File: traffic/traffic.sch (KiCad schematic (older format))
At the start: 7 parts, among them J1 Conn_01x06_Male

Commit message: changed LEds from 3mm to 5mm;added Status LED to motor-module
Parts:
- D1: renamed from D5; footprint LEDs:LED_D3.0mm -> LEDs:LED_D5.0mm
- D2: renamed from D4; footprint LEDs:LED_D3.0mm -> LEDs:LED_D5.0mm
- D3: renamed from D1; footprint LEDs:LED_D3.0mm -> LEDs:LED_D5.0mm
- D4: renamed from D3; footprint LEDs:LED_D3.0mm -> LEDs:LED_D5.0mm
- D5: renamed from D2; footprint LEDs:LED_D3.0mm -> LEDs:LED_D5.0mm
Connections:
- net labels added: +5C
- net labels removed: GND
- wire segments 23 -> 24
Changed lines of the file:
@@
 EESchema Schematic File Version 4
-LIBS:openplc_modules-cache
+LIBS:traffic-cache
 EELAYER 26 0
 EELAYER END
@@
 $EndDescr
 $Comp
-L Device:LED D5
+L Device:LED D1
 U 1 1 5C2C2999
 P 5200 4100
-F 0 "D5" H 5191 4316 50  0000 C CNN
+F 0 "D1" H 5191 4316 50  0000 C CNN
 F 1 "LED" H 5191 4225 50  0000 C CNN
-F 2 "LEDs:LED_D3.0mm" H 5200 4100 50  0001 C CNN
+F 2 "LEDs:LED_D5.0mm" H 5200 4100 50  0001 C CNN
 F 3 "~" H 5200 4100 50  0001 C CNN
 	1    5200 4100
@@
 $EndComp
 $Comp
-L Device:LED D2
+L Device:LED D5
 U 1 1 5C2C2A10
 P 5200 3050
-F 0 "D2" H 5191 3266 50  0000 C CNN
+F 0 "D5" H 5191 3266 50  0000 C CNN
 F 1 "LED" H 5191 3175 50  0000 C CNN
-F 2 "LEDs:LED_D3.0mm" H 5200 3050 50  0001 C CNN
+F 2 "LEDs:LED_D5.0mm" H 5200 3050 50  0001 C CNN
 F 3 "~" H 5200 3050 50  0001 C CNN
 	1    5200 3050
@@
 $EndComp
 $Comp
-L Device:LED D4
+L Device:LED D2
 U 1 1 5C2C2A3E
 P 5200 3750
-F 0 "D4" H 5191 3966 50  0000 C CNN
+F 0 "D2" H 5191 3966 50  0000 C CNN
 F 1 "LED" H 5191 3875 50  0000 C CNN
-F 2 "LEDs:LED_D3.0mm" H 5200 3750 50  0001 C CNN
+F 2 "LEDs:LED_D5.0mm" H 5200 3750 50  0001 C CNN
 F 3 "~" H 5200 3750 50  0001 C CNN
 	1    5200 3750
@@
 $EndComp
 $Comp
-L Device:LED D3
+L Device:LED D4
 U 1 1 5C2C2A6F
 P 5200 3400
-F 0 "D3" H 5191 3616 50  0000 C CNN
+F 0 "D4" H 5191 3616 50  0000 C CNN
 F 1 "LED" H 5191 3525 50  0000 C CNN
-F 2 "LEDs:LED_D3.0mm" H 5200 3400 50  0001 C CNN
+F 2 "LEDs:LED_D5.0mm" H 5200 3400 50  0001 C CNN
 F 3 "~" H 5200 3400 50  0001 C CNN
 	1    5200 3400
@@
 $EndComp
 $Comp
-L Device:LED D1
+L Device:LED D3
 U 1 1 5C2C2AD6
 P 5200 2700
-F 0 "D1" H 5191 2916 50  0000 C CNN
+F 0 "D3" H 5191 2916 50  0000 C CNN
 F 1 "LED" H 5191 2825 50  0000 C CNN
-F 2 "LEDs:LED_D3.0mm" H 5200 2700 50  0001 C CNN
+F 2 "LEDs:LED_D5.0mm" H 5200 2700 50  0001 C CNN
 F 3 "~" H 5200 2700 50  0001 C CNN
 	1    5200 2700
@@
 	1    0    0    -1
 $EndComp
-$Comp
-L power:GND #PWR0101
-U 1 1 5C2C3C39
-P 5050 4900
-F 0 "#PWR0101" H 5050 4650 50  0001 C CNN
-F 1 "GND" H 5055 4727 50  0000 C CNN
-F 2 "" H 5050 4900 50  0001 C CNN
-F 3 "" H 5050 4900 50  0001 C CNN
-	1    5050 4900
-	1    0    0    -1
-$EndComp
 Wire Wire Line
 	5050 4750 5050 4800
@@
 Wire Wire Line
 	5050 3750 5050 4100
+$Comp
+L power:+5C #PWR?
+U 1 1 5C32F085
+P 4700 4900
+F 0 "#PWR?" H 4700 4750 50  0001 C CNN
+F 1 "+5C" H 4715 5073 50  0000 C CNN
+F 2 "" H 4700 4900 50  0001 C CNN
+F 3 "" H 4700 4900 50  0001 C CNN
+	1    4700 4900
+	1    0    0    -1
+$EndComp
+Wire Wire Line
+	4700 4900 5050 4900
 $EndSCHEMATC

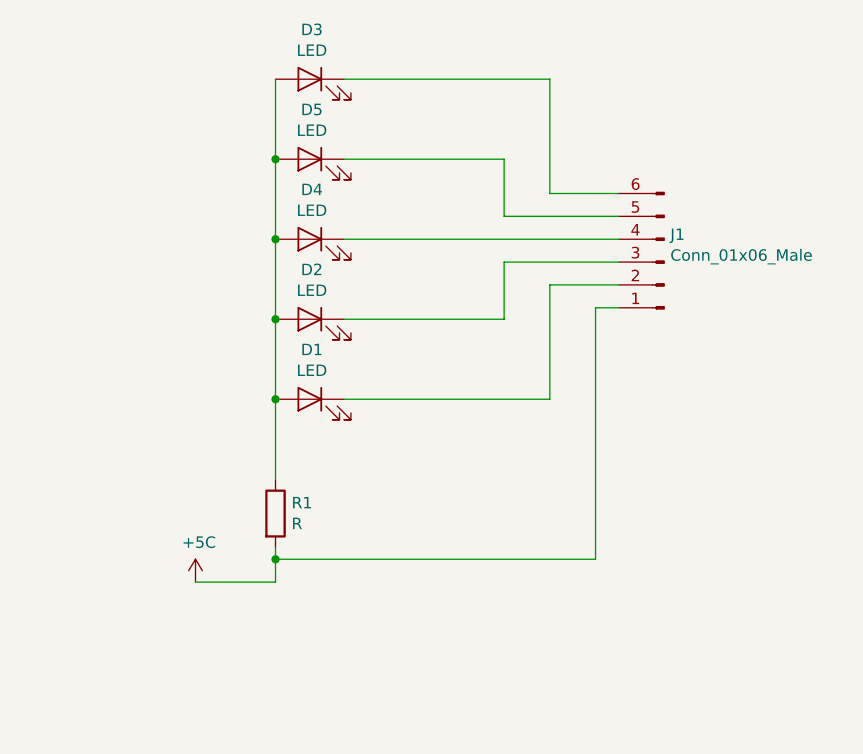
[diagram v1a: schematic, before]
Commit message: mounting holes in motor, extra pins in traffic, corrections in labels
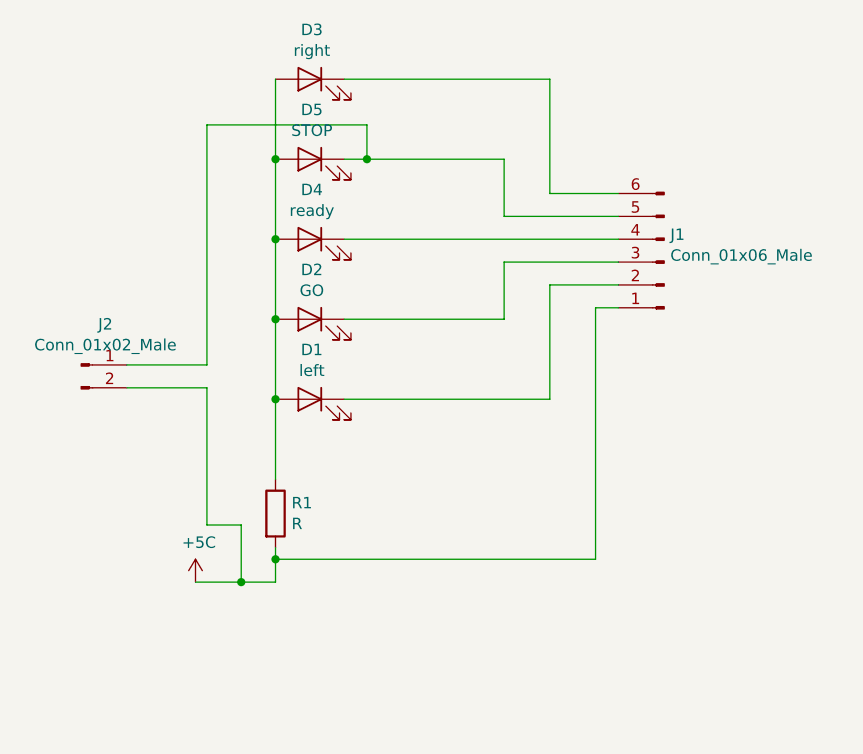
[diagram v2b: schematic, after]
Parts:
- added J2: Conn_01x02_Male, Socket_Strips:Socket_Strip_Straight_1x02_Pitch2.54mm, symbol Connector:Conn_01x02_Male
- D1: value LED -> left
- D2: value LED -> GO
- D3: value LED -> right
- D4: value LED -> ready
- D5: value LED -> STOP
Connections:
- net +5C: now also J2.2 (Pin_2)
- net at D5.1 (K), J1.5 (Pin_5): now also J2.1 (Pin_1)
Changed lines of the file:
@@
 P 5200 4100
 F 0 "D1" H 5191 4316 50  0000 C CNN
-F 1 "LED" H 5191 4225 50  0000 C CNN
+F 1 "left" H 5191 4225 50  0000 C CNN
 F 2 "LEDs:LED_D5.0mm" H 5200 4100 50  0001 C CNN
 F 3 "~" H 5200 4100 50  0001 C CNN
@@
 P 5200 3050
 F 0 "D5" H 5191 3266 50  0000 C CNN
-F 1 "LED" H 5191 3175 50  0000 C CNN
+F 1 "STOP" H 5191 3175 50  0000 C CNN
 F 2 "LEDs:LED_D5.0mm" H 5200 3050 50  0001 C CNN
 F 3 "~" H 5200 3050 50  0001 C CNN
@@
 P 5200 3750
 F 0 "D2" H 5191 3966 50  0000 C CNN
-F 1 "LED" H 5191 3875 50  0000 C CNN
+F 1 "GO" H 5191 3875 50  0000 C CNN
 F 2 "LEDs:LED_D5.0mm" H 5200 3750 50  0001 C CNN
 F 3 "~" H 5200 3750 50  0001 C CNN
@@
 P 5200 3400
 F 0 "D4" H 5191 3616 50  0000 C CNN
-F 1 "LED" H 5191 3525 50  0000 C CNN
+F 1 "ready" H 5191 3525 50  0000 C CNN
 F 2 "LEDs:LED_D5.0mm" H 5200 3400 50  0001 C CNN
 F 3 "~" H 5200 3400 50  0001 C CNN
@@
 P 5200 2700
 F 0 "D3" H 5191 2916 50  0000 C CNN
-F 1 "LED" H 5191 2825 50  0000 C CNN
+F 1 "right" H 5191 2825 50  0000 C CNN
 F 2 "LEDs:LED_D5.0mm" H 5200 2700 50  0001 C CNN
 F 3 "~" H 5200 2700 50  0001 C CNN
@@
 	6250 3200 6550 3200
 Wire Wire Line
-	5350 3050 6050 3050
+	5350 3050 5450 3050
 Wire Wire Line
 	6050 3050 6050 3300
@@
 	5050 3750 5050 4100
 $Comp
-L power:+5C #PWR?
+L power:+5C #PWR0101
 U 1 1 5C32F085
 P 4700 4900
-F 0 "#PWR?" H 4700 4750 50  0001 C CNN
+F 0 "#PWR0101" H 4700 4750 50  0001 C CNN
 F 1 "+5C" H 4715 5073 50  0000 C CNN
 F 2 "" H 4700 4900 50  0001 C CNN
@@
 $EndComp
 Wire Wire Line
-	4700 4900 5050 4900
+	4700 4900 4900 4900
+$Comp
+L Connector:Conn_01x02_Male J2
+U 1 1 5C3CB942
+P 4200 3950
+F 0 "J2" H 4306 4128 50  0000 C CNN
+F 1 "Conn_01x02_Male" H 4306 4037 50  0000 C CNN
+F 2 "Socket_Strips:Socket_Strip_Straight_1x02_Pitch2.54mm" H 4200 3950 50  0001 C CNN
+F 3 "~" H 4200 3950 50  0001 C CNN
+	1    4200 3950
+	1    0    0    -1
+$EndComp
+Wire Wire Line
+	4400 4050 4750 4050
+Wire Wire Line
+	4750 4050 4750 4650
+Wire Wire Line
+	4750 4650 4900 4650
+Wire Wire Line
+	4900 4650 4900 4900
+Connection ~ 4900 4900
+Wire Wire Line
+	4900 4900 5050 4900
+Wire Wire Line
+	4400 3950 4750 3950
+Wire Wire Line
+	4750 2900 5450 2900
+Wire Wire Line
+	5450 2900 5450 3050
+Wire Wire Line
+	4750 2900 4750 3950
+Connection ~ 5450 3050
+Wire Wire Line
+	5450 3050 6050 3050
 $EndSCHEMATC

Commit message: gerbers generate
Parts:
- added Q?: BC327, Package_TO_SOT_THT:TO-92_Inline, symbol Transistor_BJT:BC327
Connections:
- net +5C: now also Q?.3 (E); no longer J1.1 (Pin_1), R1.2
- new net: Q?.1 (C), R1.2
- new net: J1.1 (Pin_1), Q?.2 (B)
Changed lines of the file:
@@
 	1    0    0    -1
 $EndComp
-Wire Wire Line
-	5050 4750 5050 4800
 $Comp
 L Connector:Conn_01x06_Male J1
@@
 	-1   0    0    1
 $EndComp
-Wire Wire Line
-	5050 4800 6450 4800
-Wire Wire Line
-	6450 4800 6450 3700
-Connection ~ 5050 4800
-Wire Wire Line
-	5050 4800 5050 4900
 Wire Wire Line
 	6550 3700 6450 3700
@@
 	1    0    0    -1
 $EndComp
-Wire Wire Line
-	4700 4900 4900 4900
 $Comp
 L Connector:Conn_01x02_Male J2
@@
 	4400 4050 4750 4050
 Wire Wire Line
-	4750 4050 4750 4650
-Wire Wire Line
-	4750 4650 4900 4650
-Wire Wire Line
-	4900 4650 4900 4900
-Connection ~ 4900 4900
-Wire Wire Line
-	4900 4900 5050 4900
-Wire Wire Line
 	4400 3950 4750 3950
 Wire Wire Line
@@
 Wire Wire Line
 	5450 3050 6050 3050
+Wire Wire Line
+	6450 3700 6450 5150
+Wire Wire Line
+	6450 5150 5350 5150
+Wire Wire Line
+	5050 4750 5050 4950
+Wire Wire Line
+	4700 4900 4700 5500
+Wire Wire Line
+	4700 5500 5050 5500
+Wire Wire Line
+	5050 5500 5050 5350
+Connection ~ 4700 4900
+Wire Wire Line
+	4700 4900 4750 4900
+Wire Wire Line
+	4750 4050 4750 4900
+$Comp
+L Transistor_BJT:BC327 Q?
+U 1 1 5C480656
+P 5150 5150
+F 0 "Q?" H 5340 5196 50  0000 L CNN
+F 1 "BC327" H 5340 5105 50  0000 L CNN
+F 2 "Package_TO_SOT_THT:TO-92_Inline" H 5350 5075 50  0001 L CIN
+F 3 "http://www.onsemi.com/pub_link/Collateral/BC327-D.PDF" H 5150 5150 50  0001 L CNN
+	1    5150 5150
+	-1   0    0    -1
+$EndComp
 $EndSCHEMATC

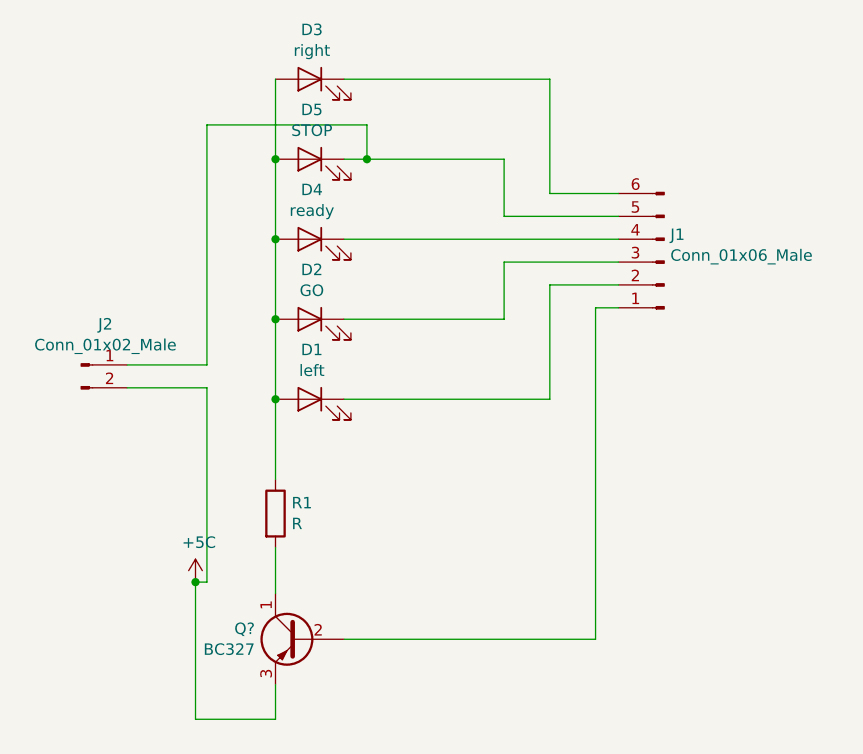
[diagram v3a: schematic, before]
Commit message: transistor driving in traffic light; updated the BOM and gerbers accordingly
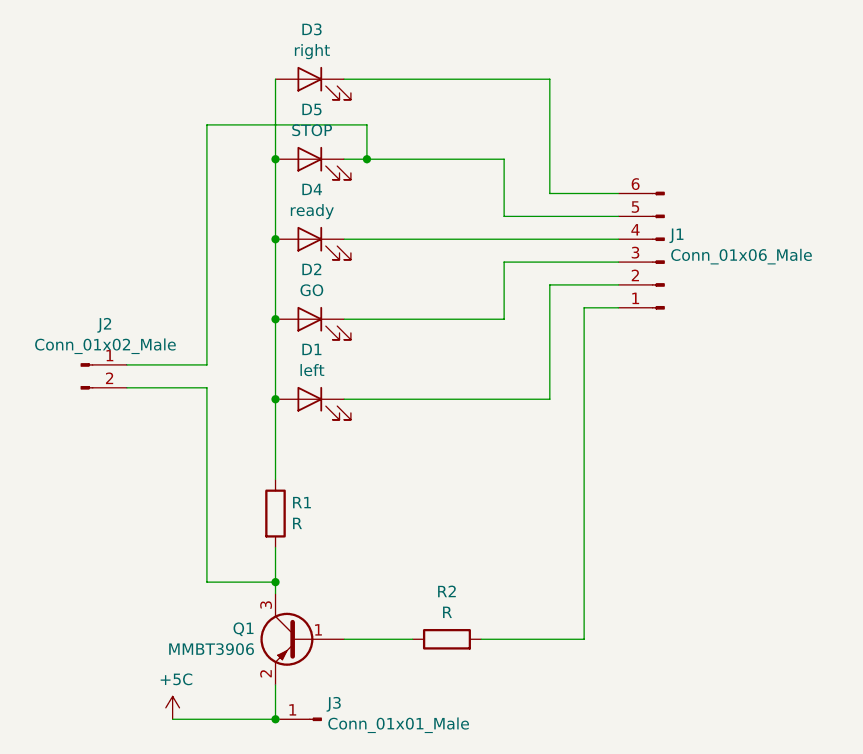
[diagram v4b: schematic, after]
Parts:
- removed Q?: BC327, Package_TO_SOT_THT:TO-92_Inline, symbol Transistor_BJT:BC327
- added J3: Conn_01x01_Male, Socket_Strips:Socket_Strip_Straight_1x01_Pitch2.54mm, symbol Connector:Conn_01x01_Male
- added Q1: MMBT3906, TO_SOT_Packages_SMD:SOT-23, symbol Transistor_BJT:MMBT3906
- added R2: R, Resistors_SMD:R_0603_HandSoldering, symbol Device:R
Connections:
- net +5C: now also J3.1 (Pin_1), Q1.2 (E); no longer J2.2 (Pin_2)
- net at R1.2: now also J2.2 (Pin_2), Q1.3 (C)
- net at J1.1 (Pin_1): now also R2.2
- new net: Q1.1 (B), R2.1
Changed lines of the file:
@@
 	1    0    0    -1
 $EndComp
-$Comp
-L Connector:Conn_01x06_Male J1
-U 1 1 5C2C6811
-P 6750 3500
-F 0 "J1" H 6723 3380 50  0000 R CNN
-F 1 "Conn_01x06_Male" H 6723 3471 50  0000 R CNN
-F 2 "Socket_Strips:Socket_Strip_Straight_1x06_Pitch2.54mm" H 6750 3500 50  0001 C CNN
-F 3 "~" H 6750 3500 50  0001 C CNN
-	1    6750 3500
-	-1   0    0    1
-$EndComp
-Wire Wire Line
-	6550 3700 6450 3700
 Connection ~ 5050 4100
 Wire Wire Line
@@
 L power:+5C #PWR0101
 U 1 1 5C32F085
-P 4700 4900
-F 0 "#PWR0101" H 4700 4750 50  0001 C CNN
-F 1 "+5C" H 4715 5073 50  0000 C CNN
-F 2 "" H 4700 4900 50  0001 C CNN
-F 3 "" H 4700 4900 50  0001 C CNN
-	1    4700 4900
+P 4600 5500
+F 0 "#PWR0101" H 4600 5350 50  0001 C CNN
+F 1 "+5C" H 4615 5673 50  0000 C CNN
+F 2 "" H 4600 5500 50  0001 C CNN
+F 3 "" H 4600 5500 50  0001 C CNN
+	1    4600 5500
 	1    0    0    -1
 $EndComp
@@
 	5450 3050 6050 3050
 Wire Wire Line
-	6450 3700 6450 5150
-Wire Wire Line
-	6450 5150 5350 5150
-Wire Wire Line
-	5050 4750 5050 4950
-Wire Wire Line
-	4700 4900 4700 5500
-Wire Wire Line
-	4700 5500 5050 5500
+	5050 4750 5050 4900
 Wire Wire Line
 	5050 5500 5050 5350
-Connection ~ 4700 4900
-Wire Wire Line
-	4700 4900 4750 4900
 Wire Wire Line
 	4750 4050 4750 4900
+Wire Wire Line
+	4750 4900 5050 4900
+Connection ~ 5050 4900
+Wire Wire Line
+	5050 4900 5050 4950
+Wire Wire Line
+	4600 5500 5050 5500
 $Comp
-L Transistor_BJT:BC327 Q?
-U 1 1 5C480656
+L Transistor_BJT:MMBT3906 Q1
+U 1 1 5C485559
 P 5150 5150
-F 0 "Q?" H 5340 5196 50  0000 L CNN
-F 1 "BC327" H 5340 5105 50  0000 L CNN
-F 2 "Package_TO_SOT_THT:TO-92_Inline" H 5350 5075 50  0001 L CIN
-F 3 "http://www.onsemi.com/pub_link/Collateral/BC327-D.PDF" H 5150 5150 50  0001 L CNN
+F 0 "Q1" H 5340 5196 50  0000 L CNN
+F 1 "MMBT3906" H 5340 5105 50  0000 L CNN
+F 2 "TO_SOT_Packages_SMD:SOT-23" H 5350 5075 50  0001 L CIN
+F 3 "https://www.fairchildsemi.com/datasheets/2N/2N3906.pdf" H 5150 5150 50  0001 L CNN
 	1    5150 5150
 	-1   0    0    -1
 $EndComp
+$Comp
+L Connector:Conn_01x06_Male J1
+U 1 1 5C2C6811
+P 6750 3500
+F 0 "J1" H 6723 3380 50  0000 R CNN
+F 1 "Conn_01x06_Male" H 6723 3471 50  0000 R CNN
+F 2 "Socket_Strips:Socket_Strip_Straight_1x06_Pitch2.54mm" H 6750 3500 50  0001 C CNN
+F 3 "~" H 6750 3500 50  0001 C CNN
+	1    6750 3500
+	-1   0    0    1
+$EndComp
+$Comp
+L Connector:Conn_01x01_Male J3
+U 1 1 5C485FD5
+P 5250 5500
+F 0 "J3" H 5223 5430 50  0000 R CNN
+F 1 "Conn_01x01_Male" H 5223 5521 50  0000 R CNN
+F 2 "Socket_Strips:Socket_Strip_Straight_1x01_Pitch2.54mm" H 5250 5500 50  0001 C CNN
+F 3 "~" H 5250 5500 50  0001 C CNN
+	1    5250 5500
+	-1   0    0    1
+$EndComp
+Connection ~ 5050 5500
+Wire Wire Line
+	6550 3700 6400 3700
+Wire Wire Line
+	6400 3700 6400 5150
+Wire Wire Line
+	6400 5150 5950 5150
+Wire Wire Line
+	5350 5150 5650 5150
+$Comp
+L Device:R R2
+U 1 1 5C48B1E4
+P 5800 5150
+F 0 "R2" V 6007 5150 50  0000 C CNN
+F 1 "R" V 5916 5150 50  0000 C CNN
+F 2 "Resistors_SMD:R_0603_HandSoldering" V 5730 5150 50  0001 C CNN
+F 3 "~" H 5800 5150 50  0001 C CNN
+	1    5800 5150
+	0    -1   -1   0
+$EndComp
 $EndSCHEMATC
